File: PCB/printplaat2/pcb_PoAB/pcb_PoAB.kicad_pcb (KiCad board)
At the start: 2 copper layers, 28.2 x 60.6 mm, 28 parts, among them J1 battertij, J2 lichtmeter1, J3 lichtmeter2, J4 lichtmeter3, J5 lichtmeter4, J6 lamp1, J7 lamp2, J8 lamp3, J9 spannigsmeter, U1 L7805CV, U2 AQY211EHAZ, U3 AQY211EHAZ, U4 AQY211EHAZ, U5 ACS712ELCTR-05B-T, U6 ACS712ELCTR-05B-T, U7 ACS712ELCTR-05B-T, U9 ARDUINO_MKR_WAN_1310

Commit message: spannings meting en bord spanning aangepast pcb en schema
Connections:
- C4 pad 2: +5V -> /5V_bord
- C5 pad 2: +5V -> /5V_bord
- C6 pad 2: +5V -> /5V_bord
- J2 pad 3: +5V -> /5V_bord
- J3 pad 3: +5V -> /5V_bord
- J4 pad 3: +5V -> /5V_bord
- J5 pad 3: +5V -> /5V_bord
- J9 pad 1: +5V -> /5V_bord
- J9 pad 5: GND -> /regelaar_in
- U1 pad 1: VCC -> /regelaar_in
- U2 pad 4: +5V -> /5V_bord
- U3 pad 4: +5V -> /5V_bord
- U4 pad 4: +5V -> /5V_bord
- U5 pad 8: +5V -> /5V_bord
- U6 pad 8: +5V -> /5V_bord
- U7 pad 8: +5V -> /5V_bord
- U9 pad J5_14: +5V -> /5V_bord
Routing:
- net /5V_bord: track 0.00 -> 184.7 mm
- net +5V: track 187.5 -> 6.13 mm
- net GND: track 236.3 -> 158.5 mm, vias 0 -> 4
- net /regelaar_in: track 0.00 -> 31.6 mm
- net VCC: track 43.5 -> 39.2 mm

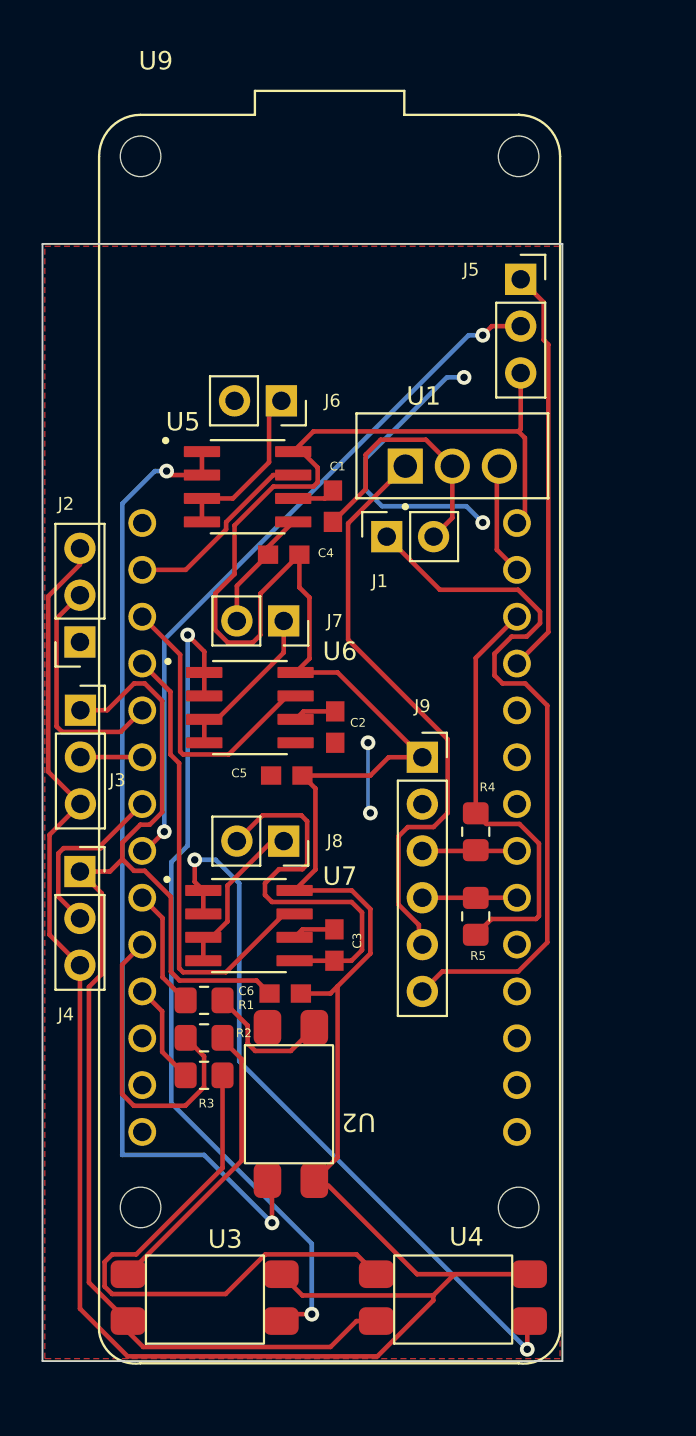
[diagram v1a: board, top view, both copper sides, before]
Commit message: PCB en schema spanning en stroommetingen aangepast
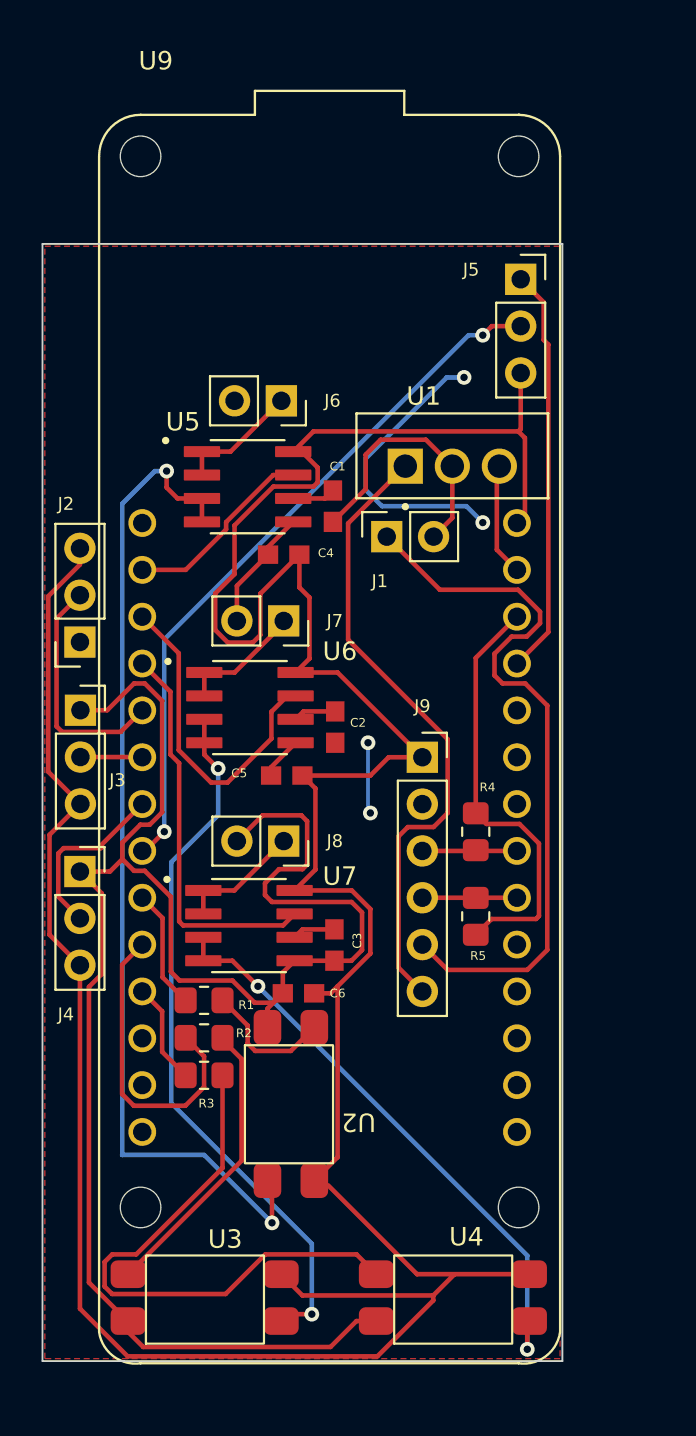
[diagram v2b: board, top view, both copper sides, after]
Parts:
- moved C6 0.72 mm to (89.3, 98.8)
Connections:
- J9 pad 5: /regelaar_in -> VCC
- J9 pad 6: VCC -> /regelaar_in
- U5 pad 1: /stroommeter1_in -> /stroommeter1_uit
- U5 pad 2: /stroommeter1_in -> /stroommeter1_uit
- U5 pad 3: /stroommeter1_uit -> /stroommeter1_in
- U5 pad 4: /stroommeter1_uit -> /stroommeter1_in
- U6 pad 1: /stroommeter2_in -> /stroommeter2_uit
- U6 pad 2: /stroommeter2_in -> /stroommeter2_uit
- U6 pad 3: /stroommeter2_uit -> /stroommeter2_in
- U6 pad 4: /stroommeter2_uit -> /stroommeter2_in
- U7 pad 1: /stroommeter3_in -> /stroommeter3_uit
- U7 pad 2: /stroommeter3_in -> /stroommeter3_uit
- U7 pad 3: /stroommeter3_uit -> /stroommeter3_in
- U7 pad 4: /stroommeter3_uit -> /stroommeter3_in
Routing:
- net /stroommeter3_in: track 39.4 -> 32.1 mm
- net /stroommeter2_in: track 45.8 -> 38.6 mm
- net GND: track 158.5 -> 165.3 mm
- net /stroom3: track 25.0 -> 21.4 mm
- net /stroommeter1_uit: track 9.33 -> 6.72 mm
- net /regelaar_in: track 31.6 -> 34.0 mm
- net /stroommeter3_uit: track 8.93 -> 6.74 mm
- net /stroom2: track 15.8 -> 17.9 mm
- net /stroommeter2_uit: track 8.79 -> 6.81 mm
- net /stroommeter1_in: track 53.8 -> 54.8 mm
- net /5V_bord: track 184.7 -> 184.0 mm

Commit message: pcb baseplate aangepast
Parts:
- added ADC_I²C1: ADS1115, ADS1115:MSOP10, F.Cu at (85.1, 61.7)
- added C7: C, Capacitor_SMD:C_0805_2012Metric_Pad1.18x1.45mm_HandSolder, F.Cu at (78.2, 62.6)
- added C8: C, Capacitor_SMD:C_0805_2012Metric_Pad1.18x1.45mm_HandSolder, F.Cu at (76.2, 62.6)
- added GPS1: GPS, Connector_PinSocket_2.54mm:PinSocket_1x04_P2.54mm_Vertical, F.Cu at (105.8, 91.0)
- added R6: R, Resistor_SMD:R_0805_2012Metric_Pad1.20x1.40mm_HandSolder, F.Cu at (81.2, 63.5)
- added R7: R, Resistor_SMD:R_0805_2012Metric_Pad1.20x1.40mm_HandSolder, F.Cu at (81.3, 61.5)
- renumbered U1 to 5V_Reg1, U5 to A_meter1, U6 to A_meter2, U7 to A_meter3, J1 to Bat1, J2 to LuxMeter1, J3 to LuxMeter2, J4 to LuxMeter3, J5 to LuxMeter4, U2 to Mos1, U3 to Mos2, U4 to Mos3, J9 to V_Meter1, J6 to lamp1, J7 to lamp2, J8 to lamp3
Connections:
- Mos1 pad 4: /5V_bord -> VCC
- Mos2 pad 4: /5V_bord -> VCC
- Mos3 pad 4: /5V_bord -> VCC
- U9 pad J3_2: /stroom1 -> unconnected-(U9-PadJ3_2)
- U9 pad J3_3: /stroom2 -> unconnected-(U9-PadJ3_3)
- U9 pad J3_4: /stroom3 -> unconnected-(U9-PadJ3_4)
- U9 pad J5_8: unconnected-(U9-PadJ5_8) -> /RX
- U9 pad J5_9: unconnected-(U9-PadJ5_9) -> /TX
- V_Meter1 pad 1: /5V_bord -> +3.3V
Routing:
- net /SCL: track 5.16 -> 77.5 mm, vias 0 -> 1
- net /SDA: track 5.14 -> 69.8 mm, vias 0 -> 1
- net VCC: track 39.5 -> 86.8 mm
- net GND: track 165.3 -> 195.8 mm, vias 4 -> 3
- net /stroom3: track 21.4 -> 49.8 mm
- net /stroom2: track 17.9 -> 33.3 mm
- net +3.3V: track 23.5 -> 29.9 mm
- net /TX: track 0.00 -> 4.61 mm
- net /RX: track 0.00 -> 4.61 mm
- net Net-(R6-Pad1): track 0.00 -> 4.40 mm
- net /5V_bord: track 184.0 -> 188.2 mm, vias 0 -> 1
- net /stroom1: track 10.6 -> 14.7 mm
- net Net-(R7-Pad2): track 0.00 -> 3.05 mm
- net /Lichtmeting4: track 38.4 -> 41.2 mm, vias 2 -> 0
- net /stroommeter1_in: track 54.8 -> 53.4 mm
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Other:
- board size 28.2 x 60.6 mm -> 33.7 x 60.2 mm

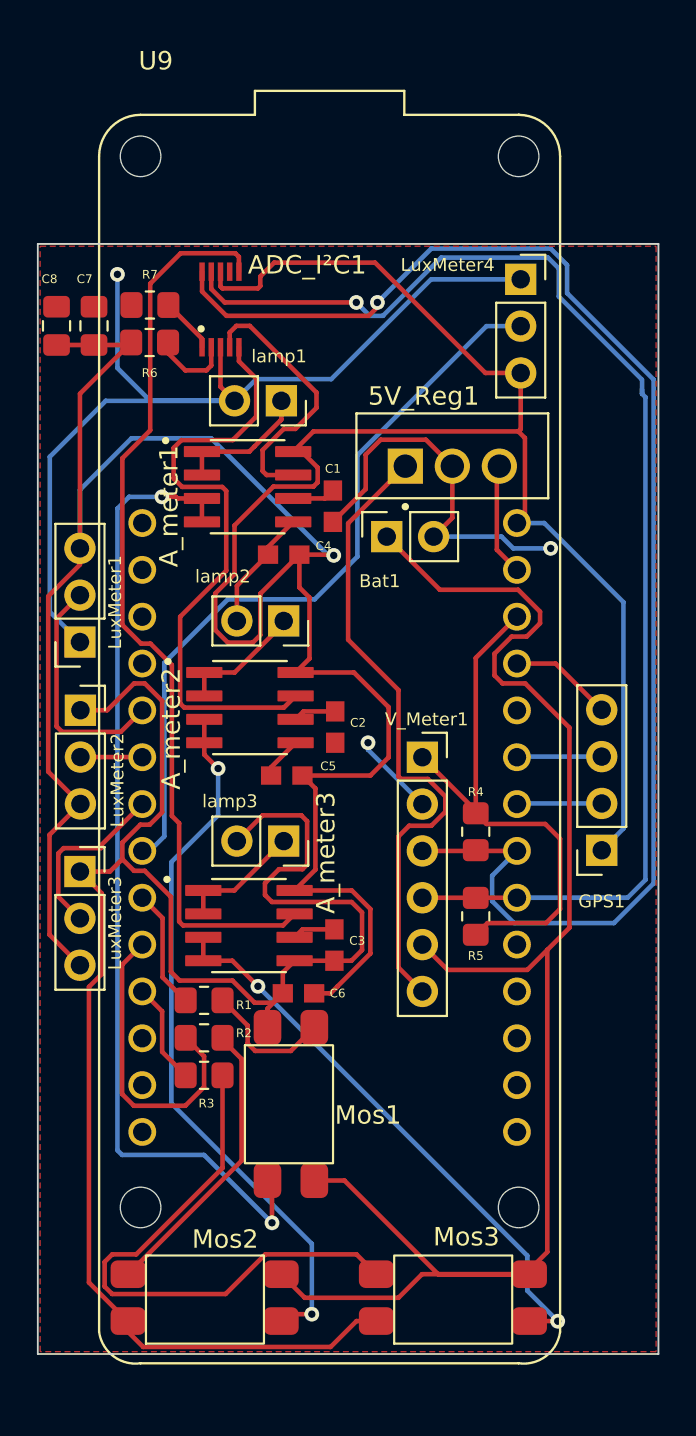
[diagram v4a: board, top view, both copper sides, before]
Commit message: PCB track width adjusted
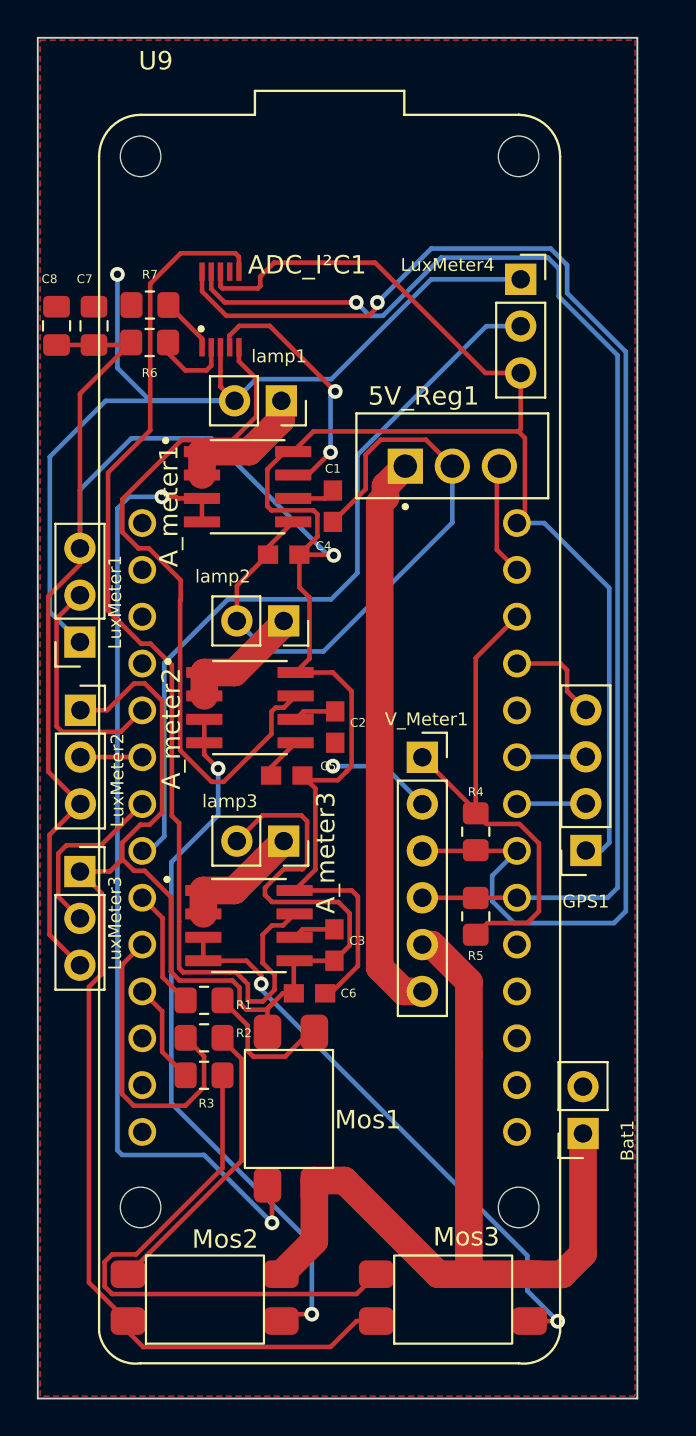
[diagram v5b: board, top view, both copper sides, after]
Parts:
- moved Bat1 34.1 mm to (104.8, 106.4), turned to 180 degrees
- moved GPS1 0.86 mm to (104.9, 91.1)
- moved C6 0.60 mm to (89.9, 98.8)
- moved Mos1 0.25 mm to (91.4, 99.6)
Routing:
- net VCC: track 86.8 -> 48.7 mm
- net /5V_bord: track 188.2 -> 171.4 mm
- net /stroom3: track 49.8 -> 58.5 mm
- net GND: track 195.8 -> 203.7 mm, vias 3 -> 2
- net /stroom2: track 33.3 -> 38.1 mm
- net /regelaar_in: track 34.7 -> 30.6 mm
- net +3.3V: track 29.9 -> 27.6 mm
- net /SDA: track 69.8 -> 67.7 mm
- net /SCL: track 77.5 -> 76.3 mm
- net Net-(R3-Pad2): track 31.1 -> 30.2 mm
- net /TX: track 4.61 -> 3.79 mm
- net /RX: track 4.61 -> 3.79 mm
- net /stroom1: track 14.7 -> 14.0 mm, vias 0 -> 2
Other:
- board size 33.7 x 60.2 mm -> 32.5 x 73.8 mm
